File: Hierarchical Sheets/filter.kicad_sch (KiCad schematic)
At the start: 2 parts

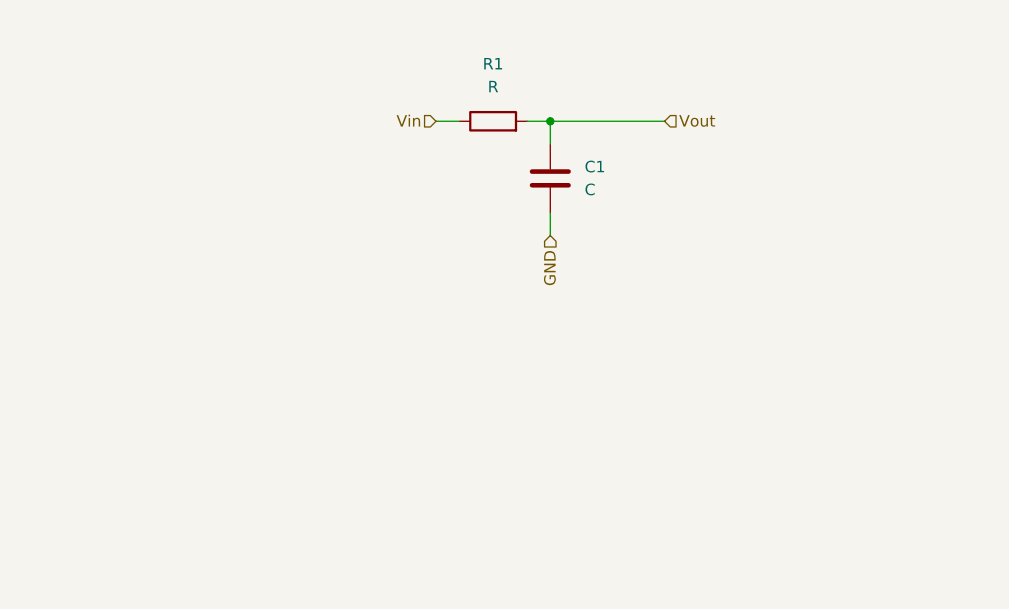
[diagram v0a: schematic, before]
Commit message: Added 2nd order low-pass filter topology - Still working on exact design
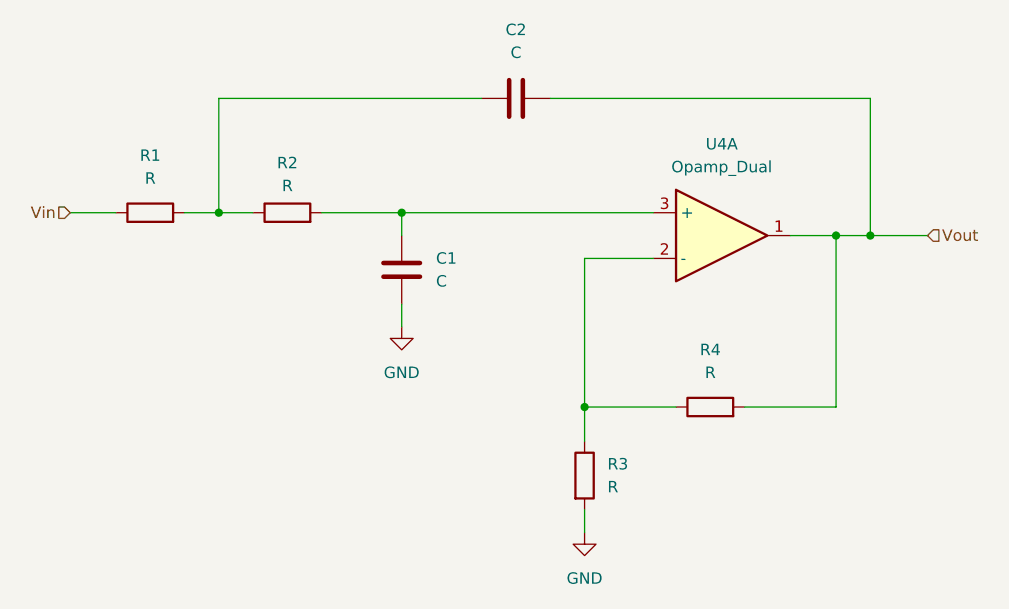
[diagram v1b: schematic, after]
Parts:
- added C2: C, symbol Device:C
- added R2, R3, R4: R, symbol Device:R
- added U4: Opamp_Dual, symbol Device:Opamp_Dual
- C1: footprint Capacitor_SMD:CP_Elec_3x5.3 -> (none)
- R1: footprint Resistor_SMD:R_0201_0603Metric_Pad0.64x0.40mm_HandSolder -> (none)
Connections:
- net GND: now also R3.2
- net Vout: now also C2.2, R4.2, U4.1; no longer C1.1, R1.2
- new net: C2.1, R1.2, R2.1
- new net: C1.1, R2.2, U4.3 (+)
- new net: R3.1, R4.1, U4.2 (-)

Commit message: Link Battery Charger
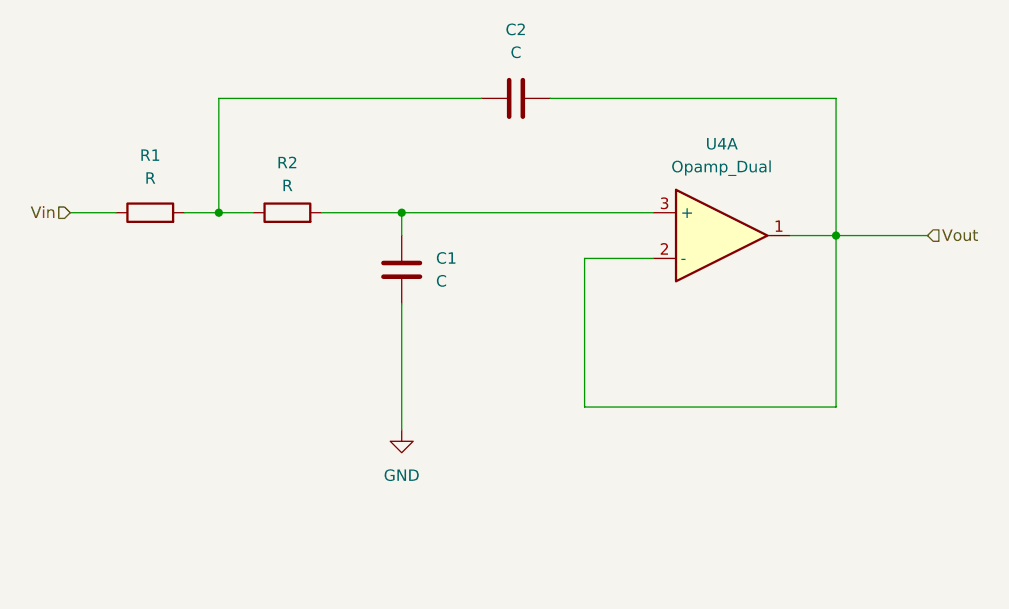
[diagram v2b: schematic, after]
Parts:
- removed R3, R4: R, symbol Device:R
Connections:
- net Vout: now also U4.2 (-)
